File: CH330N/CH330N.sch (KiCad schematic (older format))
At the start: 18 parts, among them J2 Conn_01x06, P1 USB_C_Plug_USB2.0, U1 CH330N, U2 AP2127K-3.3

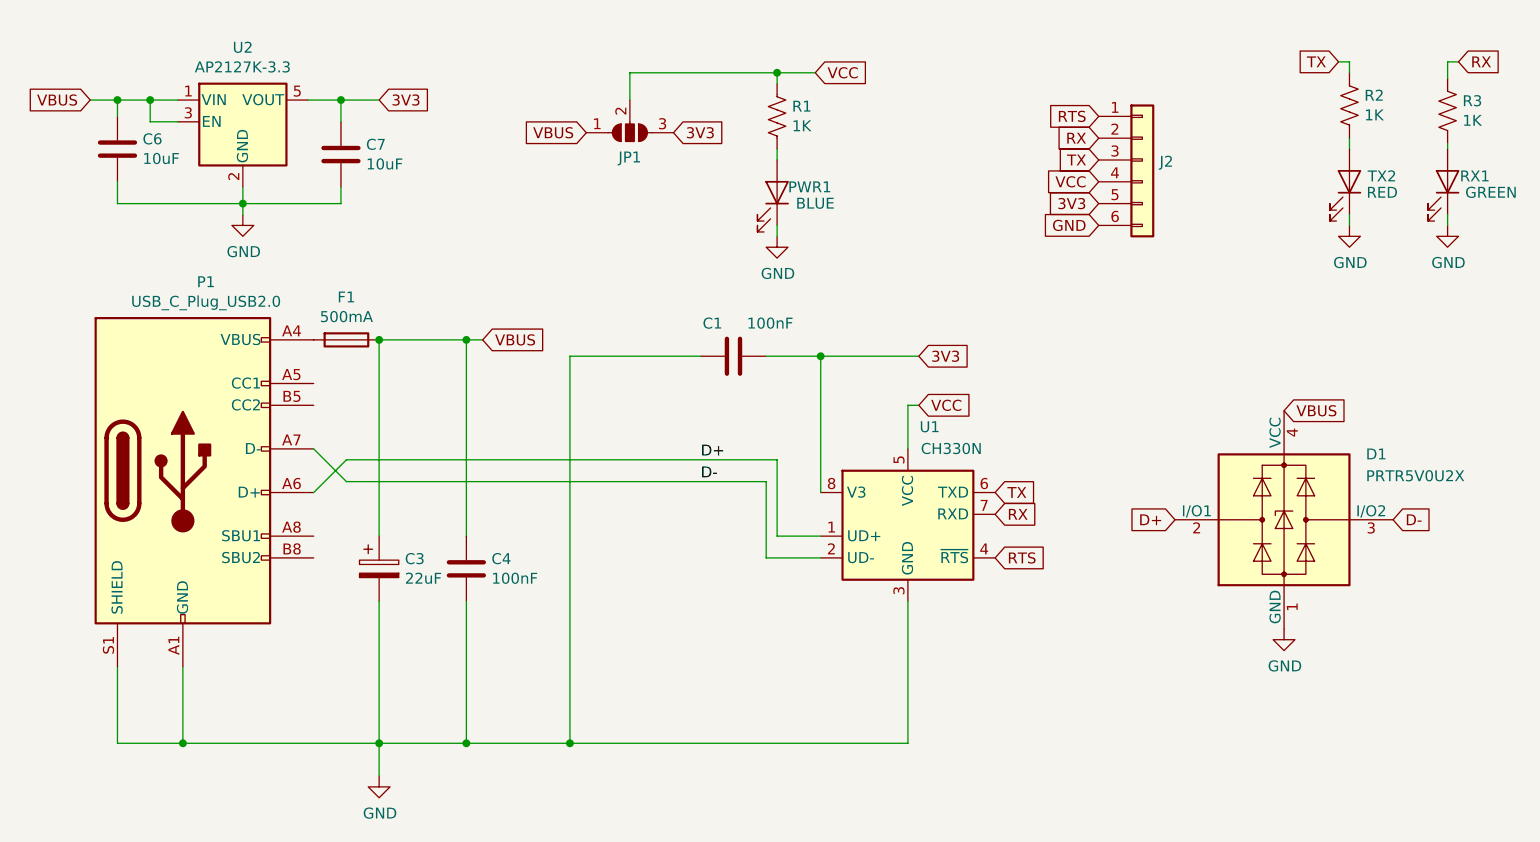
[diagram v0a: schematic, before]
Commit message: SirUSB Updates
CH330N Revision 1.1 + 3D Render Improvement
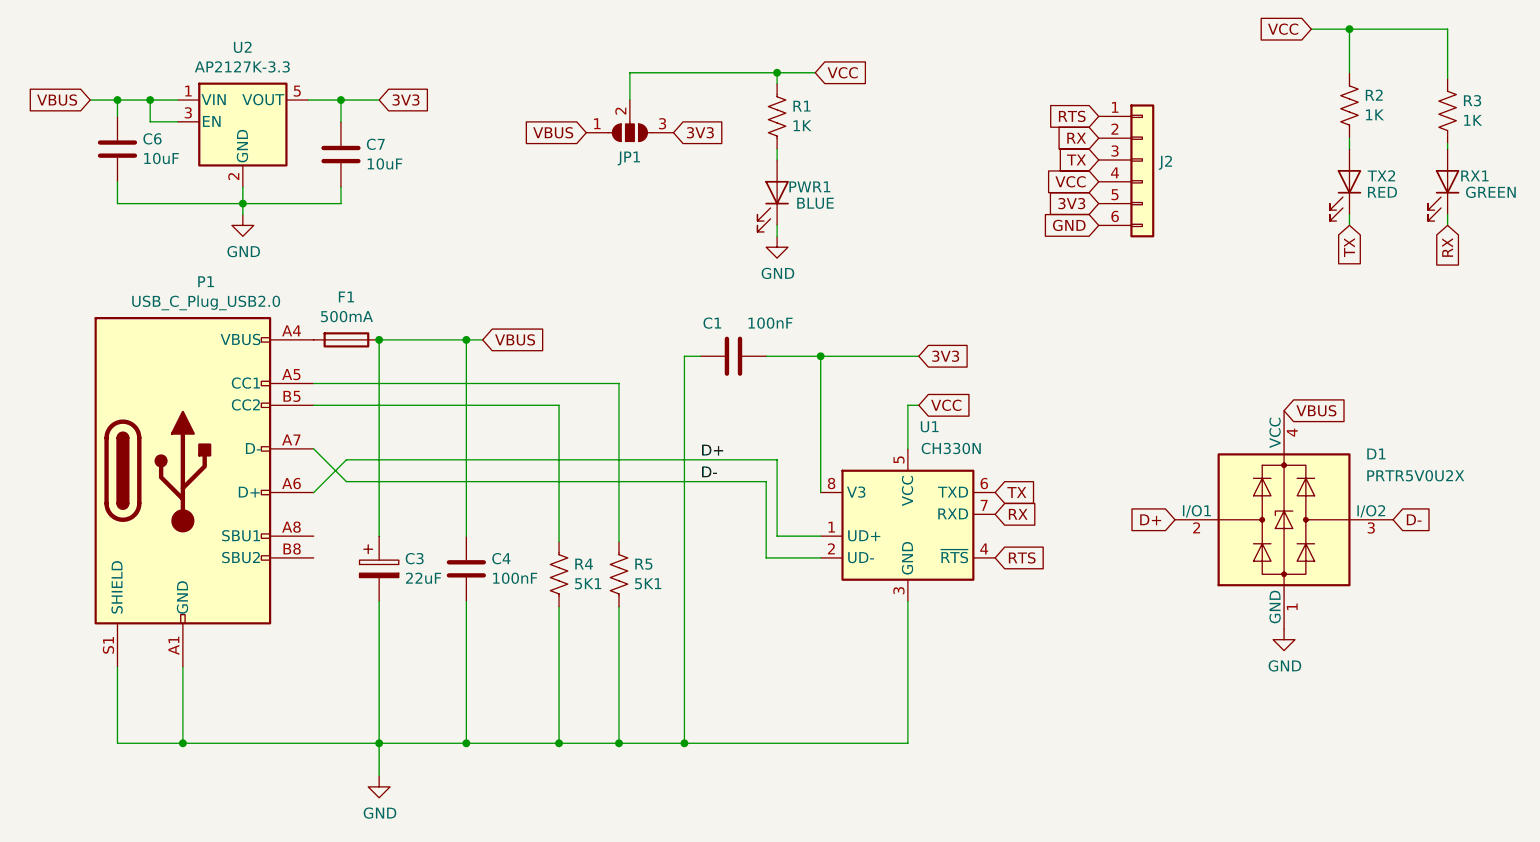
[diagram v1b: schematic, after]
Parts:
- added R4, R5: 5K1, Resistor_SMD:R_0603_1608Metric, symbol Device:R_US
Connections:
- net GND: now also R4.2, R5.2; no longer RX1.1 (K), TX2.1 (K)
- net RX: now also RX1.1 (K); no longer R3.1
- net TX: now also TX2.1 (K); no longer R2.1
- net VCC: now also R2.1, R3.1
- net at P1.A5 (CC1): now also R5.1
- net at P1.B5 (CC2): now also R4.1
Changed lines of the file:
@@
 	4375 2125 4375 2750
 Wire Wire Line
-	3825 2125 3225 2125
+	3825 2125 3750 2125
 Text GLabel 5175 3050 2    50   Input ~ 0
 RTS
@@
 Wire Wire Line
 	7250 1175 7250 1150
-$Comp
-L power:GND #PWR0103
-U 1 1 5E4C8EE3
-P 7250 1525
-F 0 "#PWR0103" H 7250 1275 50  0001 C CNN
-F 1 "GND" H 7254 1353 50  0000 C CNN
-F 2 "" H 7250 1525 50  0001 C CNN
-F 3 "" H 7250 1525 50  0001 C CNN
-	1    7250 1525
-	1    0    0    -1
-$EndComp
 Wire Wire Line
 	7250 1525 7250 1475
@@
 	1    0    0    -1
 $EndComp
-Text GLabel 7300 775  2    50   Input ~ 0
+Text GLabel 7250 1525 3    50   Input ~ 0
 RX
-Wire Wire Line
-	7300 775  7250 775
-Wire Wire Line
-	7250 775  7250 850
-Text GLabel 6750 775  0    50   Input ~ 0
+Text GLabel 6800 1525 3    50   Input ~ 0
 TX
-Wire Wire Line
-	6750 775  6800 775
 $Comp
 L Device:LED RX1
@@
 Wire Wire Line
 	6800 1525 6800 1475
-$Comp
-L power:GND #PWR0104
-U 1 1 5E4E74AC
-P 6800 1525
-F 0 "#PWR0104" H 6800 1275 50  0001 C CNN
-F 1 "GND" H 6804 1353 50  0000 C CNN
-F 2 "" H 6800 1525 50  0001 C CNN
-F 3 "" H 6800 1525 50  0001 C CNN
-	1    6800 1525
-	1    0    0    -1
-$EndComp
-Wire Wire Line
-	6800 825  6800 775
 Wire Wire Line
 	6800 1175 6800 1125
@@
 Text GLabel 4825 2125 2    50   Input ~ 0
 3V3
-Connection ~ 3225 3900
-Wire Wire Line
-	3225 2125 3225 3900
-Wire Wire Line
-	3225 3900 4775 3900
+Connection ~ 3750 3900
+Wire Wire Line
+	3750 2125 3750 3900
+Wire Wire Line
+	3750 3900 4775 3900
 Connection ~ 2750 2050
 Connection ~ 2750 3900
 Wire Wire Line
-	2750 3900 3225 3900
+	2750 3900 3175 3900
 Wire Wire Line
 	2350 2050 2750 2050
@@
 Text GLabel 5650 1425 0    50   Input ~ 0
 3V3
+Text GLabel 6625 625  0    50   Input ~ 0
+VCC
+Wire Wire Line
+	7250 850  7250 625
+Wire Wire Line
+	6625 625  6800 625
+Wire Wire Line
+	6800 625  6800 825
+Connection ~ 6800 625
+Wire Wire Line
+	6800 625  7250 625
+$Comp
+L Device:R_US R4
+U 1 1 5E9C0593
+P 3175 3125
+F 0 "R4" H 3243 3170 50  0000 L CNN
+F 1 "5K1" H 3243 3080 50  0000 L CNN
+F 2 "Resistor_SMD:R_0603_1608Metric" V 3215 3115 50  0001 C CNN
+F 3 "~" H 3175 3125 50  0001 C CNN
+F 4 "C332117" H 3175 3125 50  0001 C CNN "Part"
+	1    3175 3125
+	1    0    0    -1
+$EndComp
+$Comp
+L Device:R_US R5
+U 1 1 5E9C1822
+P 3450 3125
+F 0 "R5" H 3518 3170 50  0000 L CNN
+F 1 "5K1" H 3518 3080 50  0000 L CNN
+F 2 "Resistor_SMD:R_0603_1608Metric" V 3490 3115 50  0001 C CNN
+F 3 "~" H 3450 3125 50  0001 C CNN
+F 4 "C332117" H 3450 3125 50  0001 C CNN "Part"
+	1    3450 3125
+	1    0    0    -1
+$EndComp
+Wire Wire Line
+	2050 2350 3175 2350
+Wire Wire Line
+	3175 2350 3175 2975
+Wire Wire Line
+	2050 2250 3450 2250
+Wire Wire Line
+	3450 2250 3450 2975
+Wire Wire Line
+	3175 3275 3175 3900
+Connection ~ 3175 3900
+Wire Wire Line
+	3175 3900 3450 3900
+Wire Wire Line
+	3450 3900 3450 3275
+Connection ~ 3450 3900
+Wire Wire Line
+	3450 3900 3750 3900
 $EndSCHEMATC

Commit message: ...
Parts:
- removed C6: 10uF, Capacitor_SMD:C_0805_2012Metric, symbol Device:C
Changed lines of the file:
@@
 VBUS
-Wire Wire Line
-	1025 950  1150 950
 Wire Wire Line
 	1300 950  1300 1050
@@
 Text GLabel 5650 1525 0    50   Input ~ 0
 GND
-$Comp
-L Device:C C6
-U 1 1 5E4982E1
-P 1150 1175
-F 0 "C6" H 1265 1220 50  0000 L CNN
-F 1 "10uF" H 1265 1130 50  0000 L CNN
-F 2 "Capacitor_SMD:C_0805_2012Metric" H 1188 1025 50  0001 C CNN
-F 3 "~" H 1150 1175 50  0001 C CNN
-F 4 "C95841" H 1150 1175 50  0001 C CNN "Part"
-	1    1150 1175
-	1    0    0    -1
-$EndComp
 Wire Wire Line
 	2175 1050 2175 950
@@
 Wire Wire Line
 	2175 950  2350 950
-Wire Wire Line
-	1150 950  1150 1025
-Connection ~ 1150 950
-Wire Wire Line
-	1150 950  1300 950
-Wire Wire Line
-	1150 1325 1150 1425
-Wire Wire Line
-	1150 1425 1725 1425
 Connection ~ 1725 1425
 Wire Wire Line
@@
 Wire Wire Line
 	3450 3900 3750 3900
+Wire Wire Line
+	1025 950  1300 950
 $EndSCHEMATC
